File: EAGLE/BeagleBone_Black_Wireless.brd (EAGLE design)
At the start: 86.4 x 54.6 mm, 275 parts, among them IC1 OSD3358, IC10 TXS0108ERGYR, IC11 TXS0108ERGYR, IC12 TPS2051BDGN, IC13 SN74AUC1G74, IC14 TPD4S012DRY, IC15 TPD4S012DRY, IC17 SN74LVC2G241DCUR, IC18 TL1963ADCQR, IC19 AP2112K-1.8TRG1 3.3V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

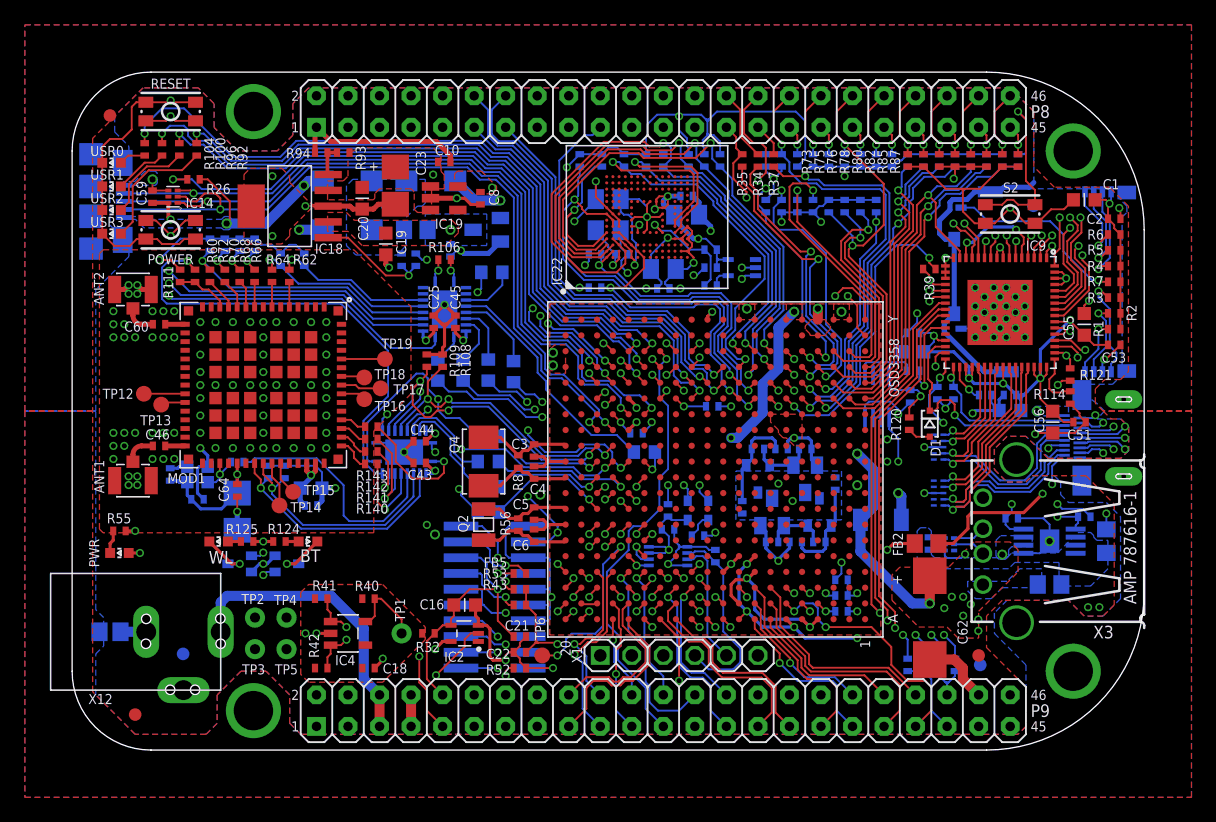
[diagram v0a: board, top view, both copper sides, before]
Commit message: PCB rev A5b: Added vias to pads
This is meant to assist in avoiding pads coming off with excess pressure.
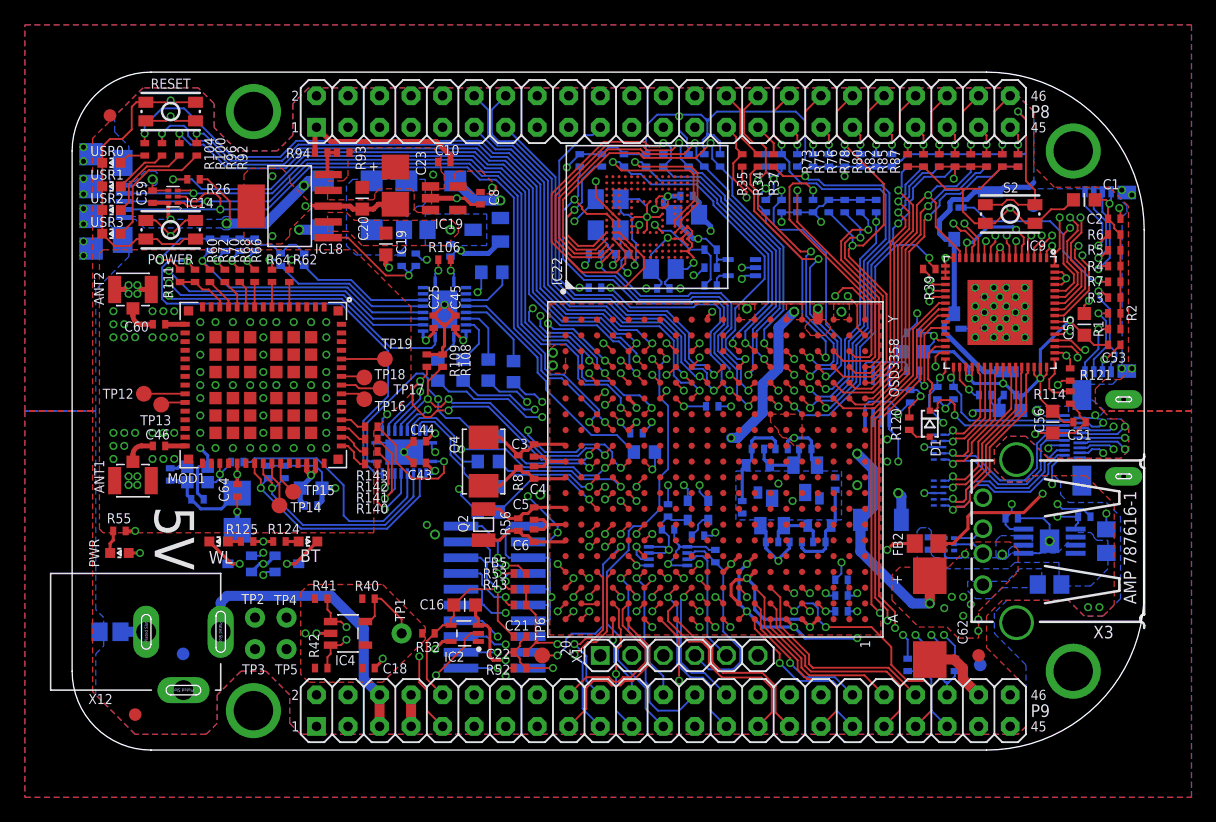
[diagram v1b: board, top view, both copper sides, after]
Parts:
- IC6: value TLVH431 (SOT-23-3) -> DNP TLVH431 (SOT-23-3)
- R48: value 499 -> DNP 499
- R50: value 10k 1% -> DNP 10k 1%
- R51: value 40.2k 1% -> DNP 40.2k 1%
- R56: value 1M, 1% -> DNP 1M, 1%
- T2: value MMBT2907 -> DNP MMBT2907
- X12: value PJ-102B_POWER_CON -> (none); device GHI:PJ-102B_POWER_CON -> GHI-Connectors:PJ-102B_POWER_CON
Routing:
- net CGND: vias 0 -> 12
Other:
- board text added: "5V"
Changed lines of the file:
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@@
 <layer number="25" name="tNames" color="7" fill="1" visible="yes" active="yes"/>
 <layer number="26" name="bNames" color="6" fill="1" visible="yes" active="yes"/>
-<layer number="27" name="tValues" color="7" fill="1" visible="no" active="yes"/>
-<layer number="28" name="bValues" color="7" fill="1" visible="no" active="yes"/>
-<layer number="29" name="tStop" color="7" fill="3" visible="yes" active="yes"/>
-<layer number="30" name="bStop" color="6" fill="6" visible="yes" active="yes"/>
+<layer number="27" name="tValues" color="7" fill="1" visible="yes" active="yes"/>
+<layer number="28" name="bValues" color="7" fill="1" visible="yes" active="yes"/>
+<layer number="29" name="tStop" color="7" fill="3" visible="no" active="yes"/>
+<layer number="30" name="bStop" color="6" fill="6" visible="no" active="yes"/>
 <layer number="31" name="tCream" color="7" fill="4" visible="no" active="yes"/>
 <layer number="32" name="bCream" color="7" fill="5" visible="no" active="yes"/>
@@
 <layer number="43" name="vRestrict" color="2" fill="10" visible="no" active="yes"/>
 <layer number="44" name="Drills" color="7" fill="1" visible="no" active="yes"/>
-<layer number="45" name="Holes" color="7" fill="1" visible="yes" active="yes"/>
+<layer number="45" name="Holes" color="7" fill="1" visible="no" active="yes"/>
 <layer number="46" name="Milling" color="3" fill="1" visible="no" active="yes"/>
 <layer number="47" name="Measures" color="63" fill="1" visible="no" active="yes"/>
@@
 <wire x1="64.262" y1="35.687" x2="64.643" y2="35.306" width="0.127" layer="22"/>
 <wire x1="64.643" y1="35.306" x2="67.056" y2="35.306" width="0.127" layer="22"/>
+<text x="6.6548" y="17.0688" size="3.175" layer="21" ratio="12" rot="SR270" align="bottom-center">5V</text>
 </plain>
 <attributes>
@@
 <attribute name="VALUE" x="53.34" y="25.019" size="1.27" layer="28" rot="MR180"/>
 </element>
-<element name="IC6" library="texas" package="DBZ_R-PDSO-G3" value="TLVH431 (SOT-23-3)" x="60.198" y="19.177" smashed="yes" rot="MR0">
+<element name="IC6" library="texas" package="DBZ_R-PDSO-G3" value="DNP TLVH431 (SOT-23-3)" x="60.198" y="19.177" smashed="yes" rot="MR0">
 <attribute name="OC_NEWARK" value="31K7146" x="60.198" y="19.177" size="1.778" layer="28" rot="MR0" display="off"/>
 <attribute name="MPN" value="LM4041DIDBZR" x="60.198" y="19.177" size="1.778" layer="28" rot="MR0" display="off"/>
@@
 <attribute name="VALUE" x="59.944" y="22.225" size="1.27" layer="28" rot="MR0"/>
 </element>
-<element name="R48" library="rcl" package="R0402" value="499" x="56.388" y="16.764" smashed="yes" rot="MR180">
+<element name="R48" library="rcl" package="R0402" value="DNP 499" x="56.388" y="16.764" smashed="yes" rot="MR180">
 <attribute name="NAME" x="54.7878" y="15.748" size="0.8128" layer="26" ratio="15" rot="MR180" align="center-left"/>
 <attribute name="VALUE" x="55.499" y="18.796" size="1.27" layer="28" rot="MR180"/>
@@
 <attribute name="VALUE" x="58.039" y="22.225" size="1.27" layer="28" rot="MR0"/>
 </element>
-<element name="R50" library="rcl" package="R0402" value="10k 1%" x="58.293" y="16.764" smashed="yes" rot="MR180">
+<element name="R50" library="rcl" package="R0402" value="DNP 10k 1%" x="58.293" y="16.764" smashed="yes" rot="MR180">
 <attribute name="NAME" x="57.0992" y="15.6464" size="0.8128" layer="26" ratio="15" rot="MR180" align="center-left"/>
 <attribute name="VALUE" x="57.404" y="18.796" size="1.27" layer="28" rot="MR180"/>
 </element>
-<element name="R51" library="rcl" package="R0402" value="40.2k 1%" x="61.468" y="21.463" smashed="yes" rot="MR90">
+<element name="R51" library="rcl" package="R0402" value="DNP 40.2k 1%" x="61.468" y="21.463" smashed="yes" rot="MR90">
 <attribute name="NAME" x="62.5856" y="20.5232" size="0.8128" layer="26" ratio="15" rot="MR90" align="center-left"/>
 <attribute name="VALUE" x="59.436" y="20.574" size="1.27" layer="28" rot="MR90"/>
@@
 <attribute name="VALUE" x="57.15" y="25.019" size="1.27" layer="28" rot="MR180"/>
 </element>
-<element name="T2" library="transistor-pnp" package="SOT23-BEC" value="MMBT2907" x="56.388" y="19.177" smashed="yes" rot="MR0">
+<element name="T2" library="transistor-pnp" package="SOT23-BEC" value="DNP MMBT2907" x="56.388" y="19.177" smashed="yes" rot="MR0">
 <attribute name="NAME" x="54.2544" y="18.5928" size="0.8128" layer="26" ratio="15" rot="MR270" align="center-left"/>
 <attribute name="VALUE" x="58.293" y="16.002" size="1.27" layer="28" rot="MR0"/>
 </element>
-<element name="X12" library="GHI" package="PJ-102B_POWER_CON" value="PJ-102B_POWER_CON" x="5.969" y="9.525" smashed="yes" rot="R180">
-<attribute name="NAME" x="3.2672" y="4.1092" size="0.8128" layer="25" ratio="15" rot="R180" align="center-left"/>
-<attribute name="VALUE" x="14.493" y="0.238" size="1.27" layer="27" rot="R90"/>
-</element>
 <element name="FUD4" library="GHI" package="FIDUCIAL_40MIL" value="FIDUCIAL" x="73.152" y="6.858" smashed="yes" rot="MR0"/>
 <element name="FUD5" library="GHI" package="FIDUCIAL_40MIL" value="FIDUCIAL" x="77.4404" y="43.8422" smashed="yes" rot="MR0"/>
@@
 <attribute name="VALUE" x="22.86" y="48.006" size="1.27" layer="27" rot="R270"/>
 </element>
-<element name="R56" library="rcl" package="R0402" value="1M, 1%" x="35.941" y="18.161" smashed="yes" rot="R90">
+<element name="R56" library="rcl" package="R0402" value="DNP 1M, 1%" x="35.941" y="18.161" smashed="yes" rot="R90">
 <attribute name="NAME" x="35.306" y="17.272" size="0.8128" layer="25" ratio="15" rot="R90"/>
 <attribute name="VALUE" x="37.973" y="17.526" size="1.27" layer="27" rot="R90"/>
 </element>
+<element name="X12" library="GHI-Connectors" package="PJ-102B_POWER_CON" value="" x="5.969" y="9.525" smashed="yes" rot="R180">
+<attribute name="NAME" x="3.2672" y="4.1092" size="0.8128" layer="25" ratio="15" rot="R180" align="center-left"/>
+<attribute name="VALUE" x="5.389" y="15.505" size="1.016" layer="27" ratio="12" rot="R180"/>
+</element>
 </elements>
 <signals>
@@
 <wire x1="25.019" y1="7.247" x2="25.019" y2="7.366" width="0.254" layer="1"/>
 <via x="25.019" y="7.366" extent="1-16" drill="0.4064"/>
-<contactref element="X12" pad="OUT"/>
 <contactref element="USR3" pad="K"/>
 <contactref element="USR2" pad="K"/>
@@
 <wire x1="82.1436" y1="24.2316" x2="81.858103125" y2="23.946103125" width="0.1524" layer="16"/>
 <wire x1="81.858103125" y1="23.946103125" x2="81.169003125" y2="23.946103125" width="0.1524" layer="16"/>
+<contactref element="X12" pad="OUT"/>
 </signal>
 <signal name="N$6">
@@
 <wire x1="41.148" y1="24.765" x2="52.705" y2="24.765" width="0.8128" layer="3"/>
 <wire x1="52.705" y1="24.765" x2="53.086" y2="25.146" width="0.8128" layer="3"/>
-<contactref element="X12" pad="IN"/>
 <via x="58.166" y="35.306" extent="1-16" drill="0.508"/>
 <wire x1="56.896" y1="30.734" x2="56.896" y2="34.036" width="0.8128" layer="16"/>
@@
 <wire x1="33.6042" y1="18.288" x2="23.495" y2="8.1788" width="0.8128" layer="15"/>
 <wire x1="23.495" y1="8.1788" x2="23.495" y2="5.715" width="0.8128" layer="15"/>
+<contactref element="X12" pad="IN"/>
 </signal>
 <signal name="PWR_BUT">
@@
 <wire x1="77.089" y1="45.339" x2="77.47" y2="45.72" width="0.4064" layer="16"/>
 <contactref element="R17" pad="2"/>
+<via x="0.9144" y="39.8272" extent="1-16" drill="0.4064" shape="square"/>
+<via x="0.9144" y="40.9702" extent="1-16" drill="0.4064" shape="square"/>
+<via x="0.9144" y="42.3672" extent="1-16" drill="0.4064" shape="square"/>
+<via x="0.9144" y="43.6118" extent="1-16" drill="0.4064" shape="square"/>
+<via x="0.9144" y="44.7802" extent="1-16" drill="0.4064" shape="square"/>
+<via x="0.9144" y="46.0248" extent="1-16" drill="0.4064" shape="square"/>
+<via x="0.9144" y="47.4218" extent="1-16" drill="0.4064" shape="square"/>
+<via x="0.9144" y="48.5648" extent="1-16" drill="0.4064" shape="square"/>
+<via x="84.5566" y="45.1104" extent="1-16" drill="0.4064" shape="square"/>
+<via x="85.3694" y="44.704" extent="1-16" drill="0.4064" shape="square"/>
+<via x="85.3694" y="30.734" extent="1-16" drill="0.4064" shape="square"/>
+<via x="84.5566" y="30.734" extent="1-16" drill="0.4064"/>
 </signal>
 <signal name="N$24">
